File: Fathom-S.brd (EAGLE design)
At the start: 112.4 x 45.7 mm, 114 parts, among them IC1 LMH6643, IC2 LMH6643, IC3 ST490AB, IC4 ST490AB, IC5 FT230XS, Q1 BC817-40W, U1 MC7812, U2 MC7805, U4 INA139, U5 MC7805, X2 USBSMD

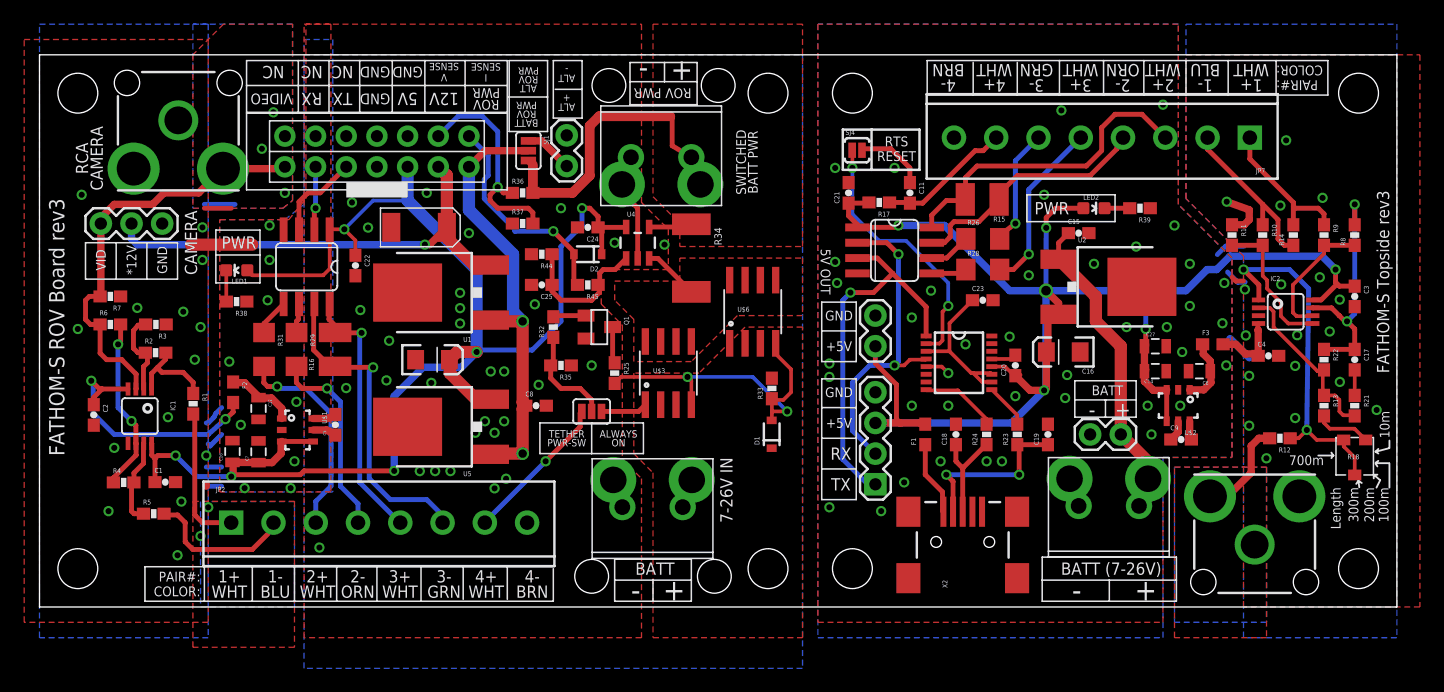
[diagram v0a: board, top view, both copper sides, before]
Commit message: Change resistor value to fix RTS reset and added more thermal vias for regulators.
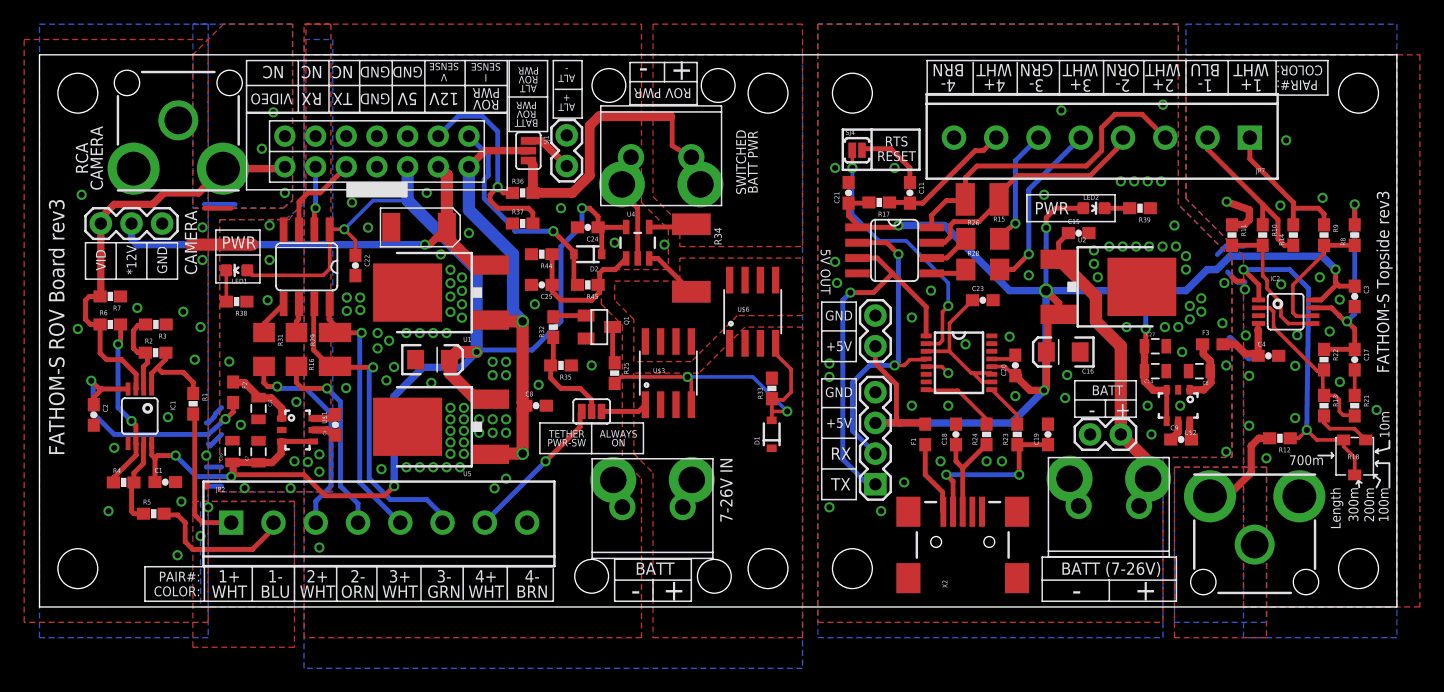
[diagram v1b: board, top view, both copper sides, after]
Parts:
- R17: value 10K -> 47K
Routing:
- net VCC-ISO: track 119.1 -> 121.3 mm
- net GND-ISO: vias 58 -> 94
- net GND: vias 58 -> 75
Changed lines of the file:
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@@
 <element name="U$12" library="BR-Eagle-Library" package="TETHER-POWER-TERMINALS" value="HEADER-2" x="86.0425" y="8.37"/>
 <element name="C11" library="SparkFun" package="0603-CAP" value="1uF" x="72.0725" y="34.29" rot="R270"/>
-<element name="R17" library="SparkFun" package="0603-RES" value="10K" x="69.5325" y="33.49625" rot="R180"/>
+<element name="R17" library="SparkFun" package="0603-RES" value="47K" x="69.5325" y="33.49625" rot="R180"/>
 <element name="SJ4" library="SparkFun-Passives" package="PAD-JUMPER-2-NC_BY_PASTE_YES_SILK" value="JUMPER-PAD-2-NC_BY_PASTE" x="67.691" y="37.8206" smashed="yes">
 <attribute name="NAME" x="66.7385" y="39.0906" size="0.4064" layer="25"/>
@@
 <wire x1="100.17125" y1="32.88665" x2="98.30435" y2="33.55975" width="0.6096" layer="1"/>
 <via x="95.25" y="24.92375" extent="1-16" drill="0.5"/>
-<via x="95.25" y="28.41625" extent="1-16" drill="0.5"/>
+<via x="94.9325" y="29.05125" extent="1-16" drill="0.5"/>
 <via x="93.98" y="31.59125" extent="1-16" drill="0.5"/>
 <via x="106.01325" y="27.29865" extent="1-16" drill="0.5"/>
@@
 <vertex x="64.4525" y="48.26"/>
 </polygon>
-<polygon width="0.4064" layer="1" isolate="0.254">
+<polygon width="0.4064" layer="1" isolate="0.254" thermals="no">
 <vertex x="64.4525" y="-1.27"/>
 <vertex x="93.0275" y="-1.27"/>
@@
 <wire x1="99.06" y1="26.9875" x2="98.7425" y2="27.305" width="0.4064" layer="1"/>
 <via x="90.01125" y="23.1775" extent="1-16" drill="0.5"/>
-<via x="93.345" y="23.1775" extent="1-16" drill="0.5"/>
+<via x="93.18625" y="23.1775" extent="1-16" drill="0.5"/>
 <via x="98.26625" y="20.0025" extent="1-16" drill="0.5"/>
+<via x="91.88" y="29.84875" extent="1-16" drill="0.5"/>
+<via x="92.99125" y="29.84875" extent="1-16" drill="0.5"/>
+<via x="94.1025" y="29.84875" extent="1-16" drill="0.5"/>
+<via x="89.69375" y="29.845" extent="1-16" drill="0.5"/>
+<via x="88.5825" y="29.845" extent="1-16" drill="0.5"/>
+<via x="87.3125" y="29.5275" extent="1-16" drill="0.5"/>
+<via x="87.63" y="27.305" extent="1-16" drill="0.5"/>
+<via x="94.9325" y="27.94" extent="1-16" drill="0.5"/>
+<via x="95.25" y="23.8125" extent="1-16" drill="0.5"/>
+<via x="94.2975" y="23.1775" extent="1-16" drill="0.5"/>
+<via x="96.2025" y="24.4475" extent="1-16" drill="0.5"/>
+<via x="96.2025" y="25.55875" extent="1-16" drill="0.5"/>
+<via x="98.26625" y="12.85875" extent="1-16" drill="0.5"/>
+<via x="89.535" y="35.2425" extent="1-16" drill="0.5"/>
+<via x="90.64625" y="35.2425" extent="1-16" drill="0.5"/>
+<via x="91.7575" y="35.2425" extent="1-16" drill="0.5"/>
+<via x="92.86875" y="35.2425" extent="1-16" drill="0.5"/>
 </signal>
 <signal name="N$10">
@@
 <contactref element="U$11" pad="2B"/>
 <contactref element="U$11" pad="2A"/>
-<polygon width="0.4064" layer="1" isolate="0.254">
+<polygon width="0.4064" layer="1" isolate="0.254" thermals="no">
 <vertex x="21.9075" y="48.26"/>
 <vertex x="49.8475" y="48.26"/>
@@
 <via x="26.5684" y="24.5872" extent="1-16" drill="0.5"/>
 <via x="28.94965" y="22.0472" extent="1-16" drill="0.5"/>
-<via x="37.3634" y="19.5072" extent="1-16" drill="0.5"/>
+<via x="37.52215" y="20.30095" extent="1-16" drill="0.5"/>
 <via x="32.44215" y="18.5547" extent="1-16" drill="0.5"/>
-<via x="31.48965" y="11.2522" extent="1-16" drill="0.5"/>
-<via x="32.75965" y="11.2522" extent="1-16" drill="0.5"/>
+<via x="30.3784" y="11.5697" extent="1-16" drill="0.5"/>
+<via x="31.48965" y="11.5697" extent="1-16" drill="0.5"/>
 <via x="41.33215" y="18.39595" extent="1-16" drill="0.5"/>
 <via x="41.01465" y="25.06345" extent="1-16" drill="0.5"/>
-<via x="34.8234" y="26.01595" extent="1-16" drill="0.5"/>
+<via x="34.98215" y="26.1747" extent="1-16" drill="0.5"/>
 <via x="51.7525" y="30.00375" extent="1-16" drill="0.5"/>
 <via x="23.1775" y="4.92125" extent="1-16" drill="0.5"/>
@@
 <via x="37.6809" y="9.82345" extent="1-16" drill="0.5"/>
 <via x="38.6334" y="10.6172" extent="1-16" drill="0.5"/>
-<via x="38.47465" y="15.3797" extent="1-16" drill="0.5"/>
-<via x="37.6809" y="14.4272" extent="1-16" drill="0.5"/>
-<via x="36.88715" y="15.3797" extent="1-16" drill="0.5"/>
-<via x="36.0934" y="14.4272" extent="1-16" drill="0.5"/>
-<via x="34.02965" y="11.2522" extent="1-16" drill="0.5"/>
-<via x="34.8234" y="24.74595" extent="1-16" drill="0.5"/>
-<via x="34.8234" y="23.47595" extent="1-16" drill="0.5"/>
-<via x="38.47465" y="19.5072" extent="1-16" drill="0.5"/>
+<via x="37.52215" y="15.53845" extent="1-16" drill="0.5"/>
+<via x="37.52215" y="14.4272" extent="1-16" drill="0.5"/>
+<via x="36.4109" y="15.53845" extent="1-16" drill="0.5"/>
+<via x="36.4109" y="14.4272" extent="1-16" drill="0.5"/>
+<via x="32.6009" y="11.5697" extent="1-16" drill="0.5"/>
+<via x="34.98215" y="25.06345" extent="1-16" drill="0.5"/>
+<via x="34.98215" y="23.9522" extent="1-16" drill="0.5"/>
+<via x="38.6334" y="20.30095" extent="1-16" drill="0.5"/>
 <polygon width="0.4064" layer="16" isolate="0.254">
 <vertex x="14.9225" y="9.525"/>
@@
 <via x="18.415" y="37.94125" extent="1-16" drill="0.5"/>
 <via x="19.05" y="28.73375" extent="1-16" drill="0.5"/>
+<via x="26.5559" y="25.6222" extent="1-16" drill="0.5"/>
+<via x="25.44465" y="25.6222" extent="1-16" drill="0.5"/>
+<via x="25.44465" y="24.51095" extent="1-16" drill="0.5"/>
+<via x="27.99715" y="22.6822" extent="1-16" drill="0.5"/>
+<via x="27.99715" y="21.4122" extent="1-16" drill="0.5"/>
+<via x="29.3624" y="19.8755" extent="1-16" drill="0.5"/>
+<via x="34.98215" y="27.28595" extent="1-16" drill="0.5"/>
+<via x="35.1409" y="15.53845" extent="1-16" drill="0.5"/>
+<via x="34.02965" y="14.58595" extent="1-16" drill="0.5"/>
+<via x="35.1409" y="14.58595" extent="1-16" drill="0.5"/>
+<via x="35.1409" y="16.49095" extent="1-16" drill="0.5"/>
+<via x="34.02965" y="13.63345" extent="1-16" drill="0.5"/>
+<via x="34.02965" y="16.49095" extent="1-16" drill="0.5"/>
+<via x="34.02965" y="15.53845" extent="1-16" drill="0.5"/>
+<via x="35.1409" y="13.63345" extent="1-16" drill="0.5"/>
+<via x="35.1409" y="12.68095" extent="1-16" drill="0.5"/>
+<via x="34.02965" y="12.68095" extent="1-16" drill="0.5"/>
+<via x="38.6334" y="15.53845" extent="1-16" drill="0.5"/>
+<via x="38.6334" y="14.4272" extent="1-16" drill="0.5"/>
+<via x="34.02965" y="27.92095" extent="1-16" drill="0.5"/>
+<via x="34.02965" y="26.8097" extent="1-16" drill="0.5"/>
+<via x="34.02965" y="25.69845" extent="1-16" drill="0.5"/>
+<via x="34.02965" y="24.42845" extent="1-16" drill="0.5"/>
+<via x="30.3784" y="22.6822" extent="1-16" drill="0.5"/>
+<via x="31.48965" y="22.6822" extent="1-16" drill="0.5"/>
+<via x="32.6009" y="22.6822" extent="1-16" drill="0.5"/>
+<via x="33.71215" y="22.6822" extent="1-16" drill="0.5"/>
+<via x="33.2359" y="29.19095" extent="1-16" drill="0.5"/>
+<via x="37.52215" y="19.1897" extent="1-16" drill="0.5"/>
+<via x="38.6334" y="19.1897" extent="1-16" drill="0.5"/>
+<via x="28.31465" y="11.41095" extent="1-16" drill="0.5"/>
+<via x="22.22215" y="11.9997" extent="1-16" drill="0.5"/>
+<via x="23.17465" y="12.6347" extent="1-16" drill="0.5"/>
+<via x="23.17465" y="11.20595" extent="1-16" drill="0.5"/>
+<via x="33.71215" y="11.5697" extent="1-16" drill="0.5"/>
+<via x="34.8234" y="11.5697" extent="1-16" drill="0.5"/>
 </signal>
 <signal name="VCC-ISO">
@@
 <wire x1="22.6614" y1="13.7058" x2="20.0614" y2="13.7058" width="0.4064" layer="1"/>
 <wire x1="18.1466" y1="11.9634" x2="18.1356" y2="11.9524" width="0.6096" layer="1"/>
-<via x="29.36875" y="11.27125" extent="1-16" drill="0.5"/>
-<wire x1="29.36875" y1="11.27125" x2="29.36875" y2="17.4625" width="0.6096" layer="16"/>
+<via x="29.36875" y="10.00125" extent="1-16" drill="0.5"/>
+<wire x1="29.36875" y1="10.00125" x2="29.36875" y2="17.4625" width="0.6096" layer="16"/>
 <wire x1="29.36875" y1="17.4625" x2="31.75" y2="19.84375" width="0.6096" layer="16"/>
 <wire x1="31.75" y1="19.84375" x2="34.925" y2="19.84375" width="0.6096" layer="16"/>
@@
 <wire x1="11.27125" y1="12.54125" x2="9.79985" y2="12.54125" width="0.4064" layer="1"/>
 <wire x1="9.79985" y1="12.54125" x2="9.564" y2="12.3054" width="0.4064" layer="1"/>
-<wire x1="29.36875" y1="11.27125" x2="21.9075" y2="11.27125" width="0.4064" layer="1"/>
-<wire x1="21.9075" y1="11.27125" x2="21.59" y2="10.95375" width="0.4064" layer="1"/>
-<wire x1="21.59" y1="10.95375" x2="16.03375" y2="10.95375" width="0.4064" layer="1"/>
+<wire x1="21.9075" y1="10.95375" x2="16.03375" y2="10.95375" width="0.4064" layer="1"/>
 <wire x1="16.03375" y1="10.95375" x2="15.875" y2="10.795" width="0.6096" layer="1"/>
 <via x="15.875" y="10.795" extent="1-16" drill="0.5"/>
@@
 <wire x1="16.03375" y1="10.95375" x2="16.03375" y2="11.9143" width="0.6096" layer="1"/>
 <wire x1="16.03375" y1="11.9143" x2="15.9766" y2="11.97145" width="0.6096" layer="1"/>
+<wire x1="21.9075" y1="10.95375" x2="23.65375" y2="9.2075" width="0.4064" layer="1"/>
+<wire x1="23.65375" y1="9.2075" x2="28.575" y2="9.2075" width="0.4064" layer="1"/>
+<wire x1="28.575" y1="9.2075" x2="29.36875" y2="10.00125" width="0.4064" layer="1"/>
 </signal>
 <signal name="ROV-TP1-">

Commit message: Changed jumpers from solder to headers. This rev4 and the beta boards will be ordered from this commit.
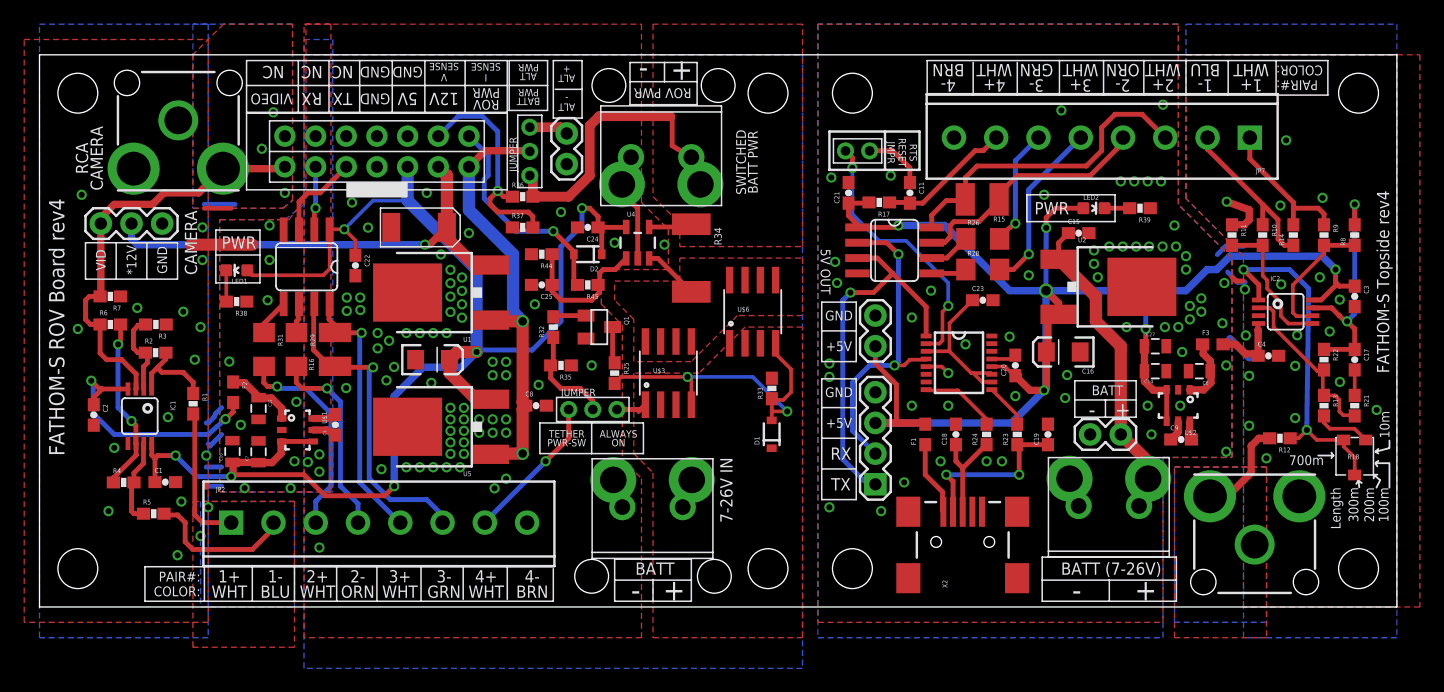
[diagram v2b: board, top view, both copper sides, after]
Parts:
- removed SJ1, SJ2: (no value), SparkFun-Passives:PAD-JUMPER-3-2OF3_NC_BY_PASTE_YES_SILK_FULL_BOX
- removed SJ4: JUMPER-PAD-2-NC_BY_PASTE, SparkFun-Passives:PAD-JUMPER-2-NC_BY_PASTE_YES_SILK
- added U$13, U$14: HEADER-33MM, BlueRobotics-Main:HEADER-2MM-3POS
- added U$16: HEADER-22MM, BlueRobotics-Main:HEADER-2MM-2POS
- moved JP10 2.70 mm to (43.7, 39.2), turned to 270 degrees
- moved R36 0.32 mm to (40.0, 34.0)
- moved R37 0.32 mm to (40.0, 31.4)
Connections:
- net N$7: now also U$16.P$1; no longer SJ4.2
- net ROV-ALT-VIN: now also U$14.P$3; no longer SJ1.1
- net ROV-BATT: now also U$13.P$3; no longer SJ2.1
- net ROV-ON: now also U$13.P$1; no longer SJ2.3
- net ROV-ON-SELECT: now also U$13.P$2; no longer SJ2.2
- net ROV-VIN: now also U$14.P$2; no longer SJ1.2
- net ROV-VIN-SWITCHED: now also U$14.P$1; no longer SJ1.3
- net RTS: now also U$16.P$2; no longer SJ4.1
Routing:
- net ROV-VIN-SWITCHED: track 27.2 -> 26.4 mm
- net ROV-ALT-VIN: track 4.04 -> 3.27 mm
- net N$7: track 5.89 -> 5.15 mm
- net ROV-BATT: track 3.86 -> 3.31 mm
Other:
- board text added: "12/15"
- board text added: "ALT PWR"
- board text added: "BATT PWR"
- board text added: "FATHOM-S ROV Board rev4"
- board text added: "FATHOM-S Topside rev4"
- board text added: "JUMPER"
- board text added: "RTS RESET JMPR"
- board text removed: "11/15"
- board text removed: "ALT ROV PWR"
- board text removed: "BATT ROV PWR"
- board text removed: "FATHOM-S ROV Board rev3"
- board text removed: "FATHOM-S Topside rev3"
- board text removed: "RTS RESET"
